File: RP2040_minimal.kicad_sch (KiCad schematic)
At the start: 34 parts

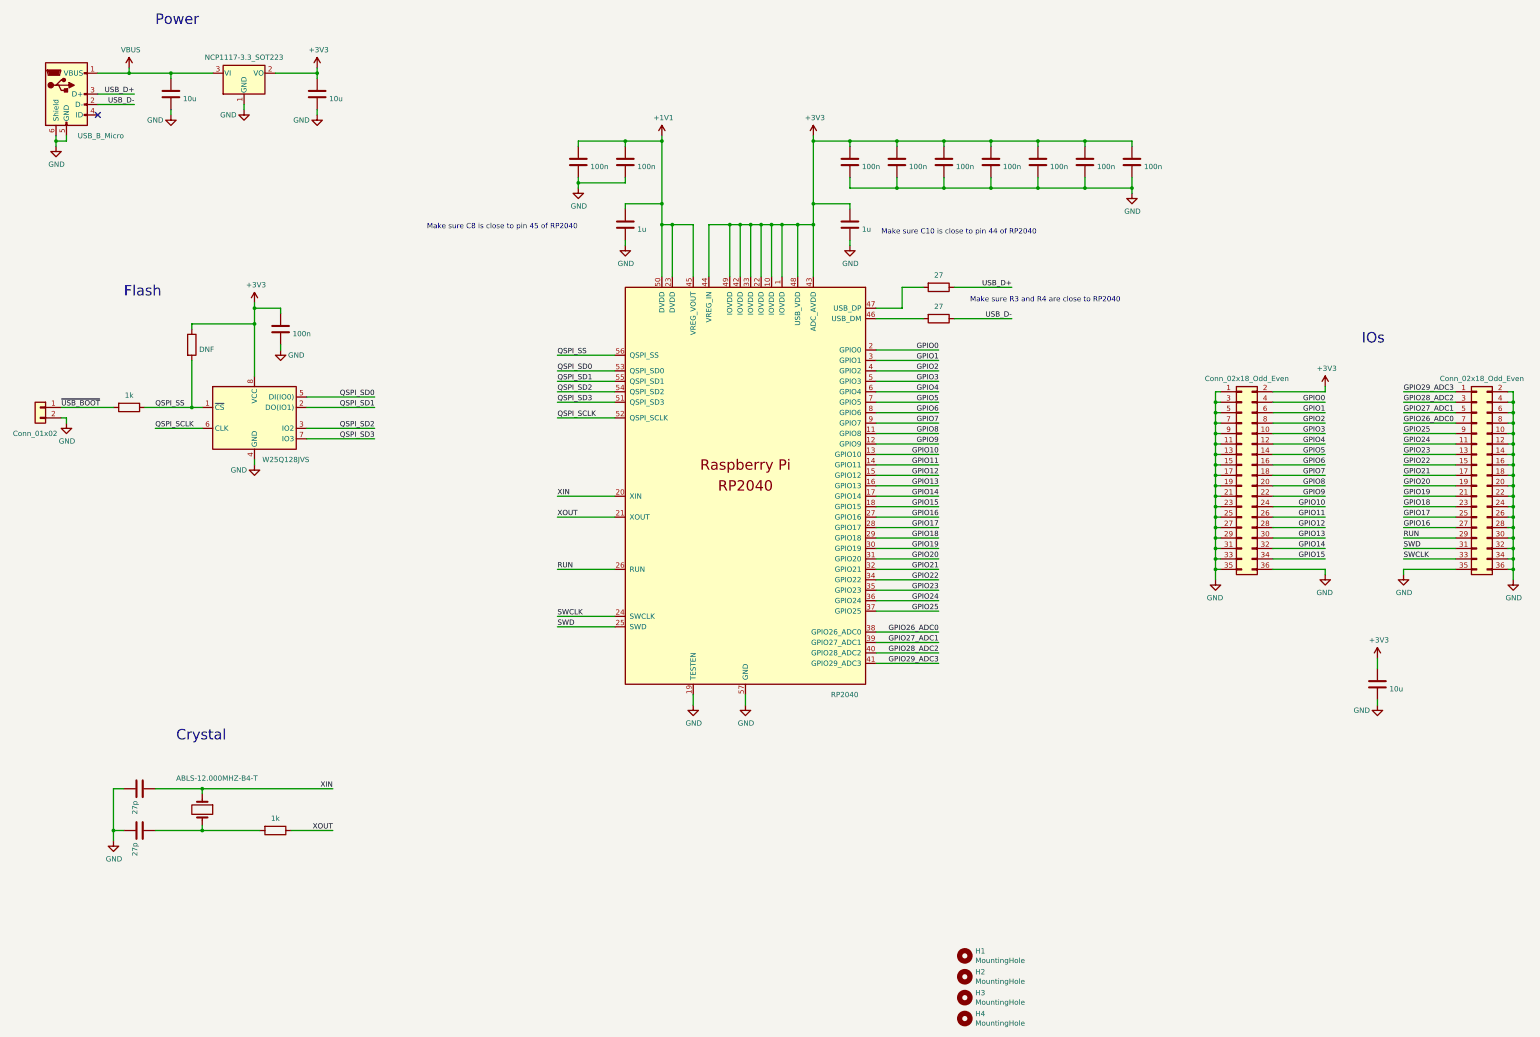
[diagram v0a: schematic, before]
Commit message: Updated sheet information, renumbered annotation for capacitors.
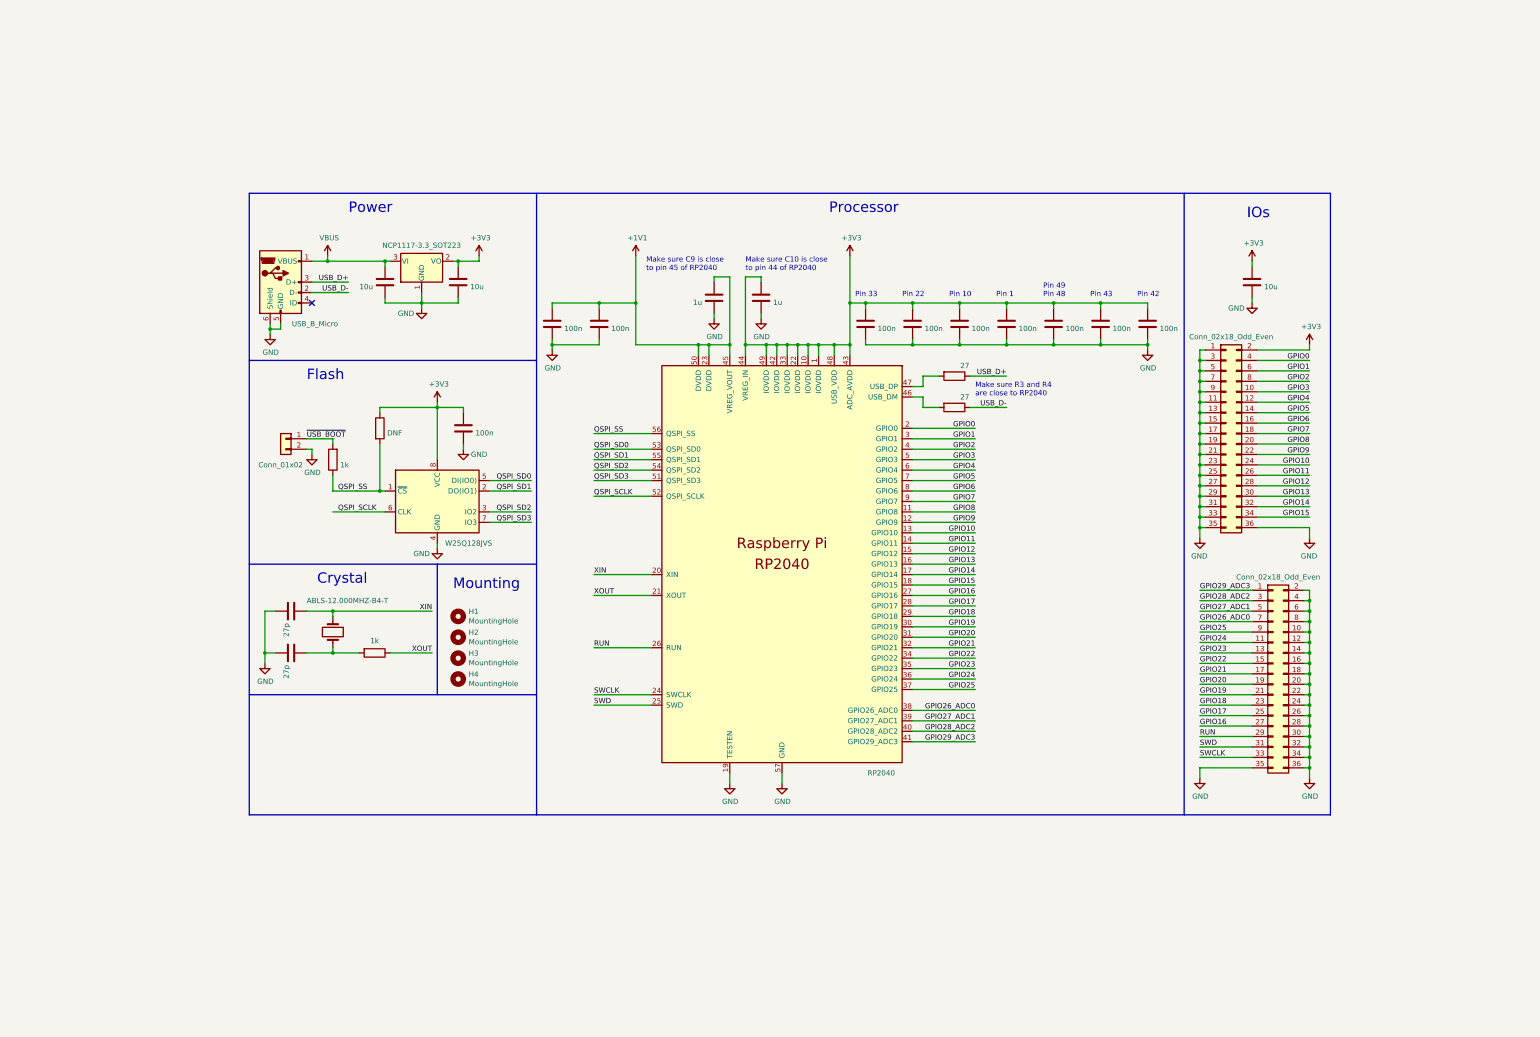
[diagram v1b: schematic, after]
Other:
- note added: "Make sure C9 is close to pin 45 of RP2040"
- note added: "Mounting"
- note added: "Pin 1"
- note added: "Pin 10"
- note added: "Pin 22"
- note added: "Pin 33"
- note added: "Pin 42"
- note added: "Pin 43"
- note added: "Pin 49 Pin 48"
- note added: "Processor"
- note removed: "Make sure C8 is close to pin 45 of RP2040"
- company: Raspberry Pi (Trading) Ltd -> AET Tech
- moved on the sheet: H1, H2, H3, H4

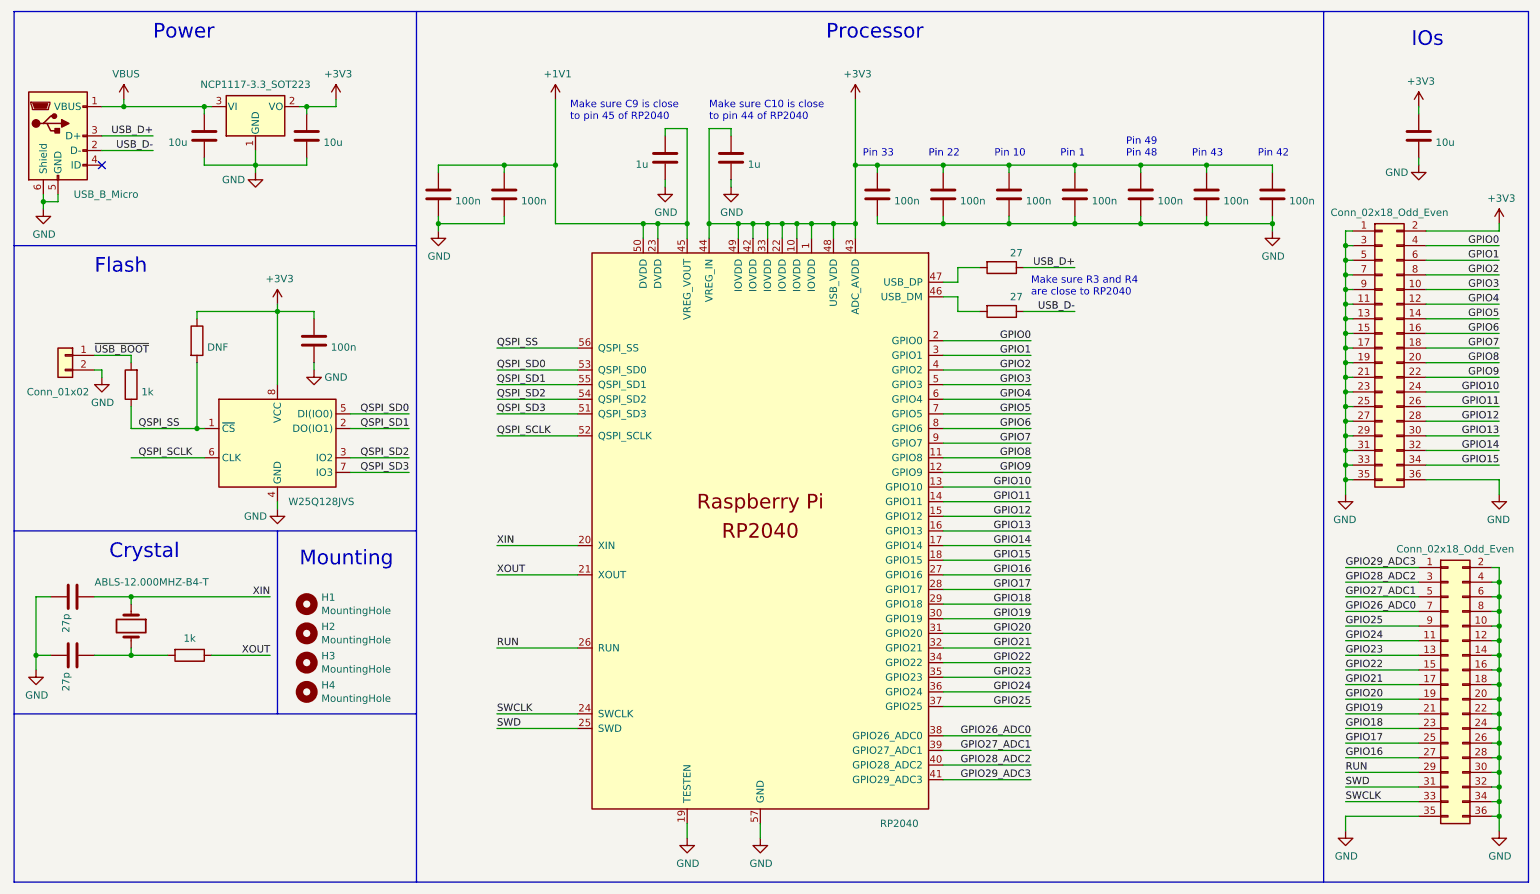
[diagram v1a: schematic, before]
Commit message: Replaced USB Micro A receptacle with USB C Added 5k1 resistors for UFP identification Added jumpers connecting CC1 to GPIO21, CC2 to GPIO22, SBU2 to GPIO0,   and SBU2 to GPIO1. Added jumper for VBUS
Updated README.md
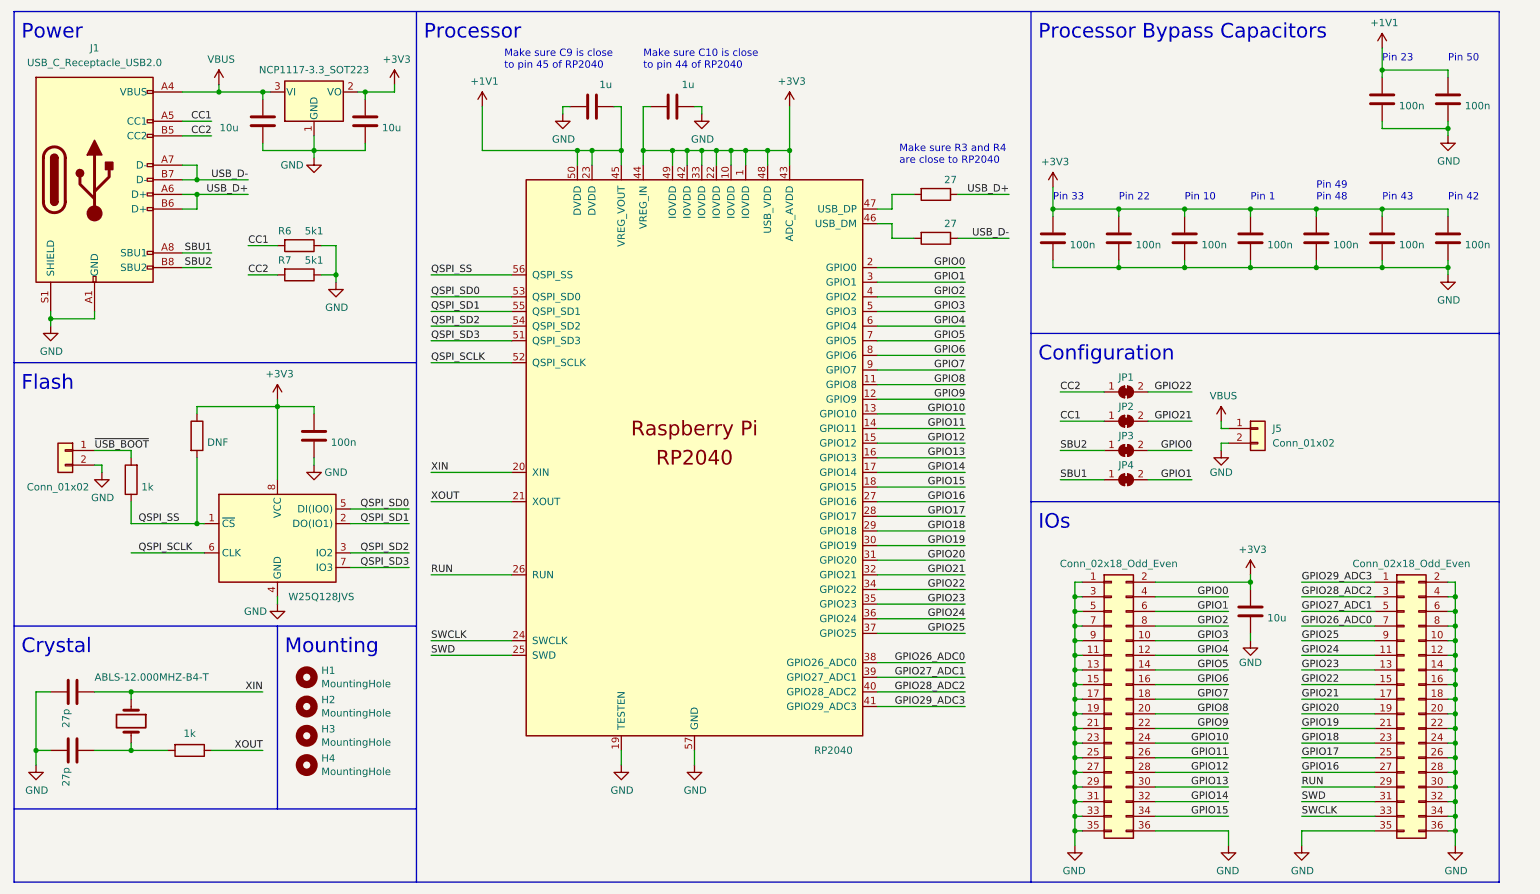
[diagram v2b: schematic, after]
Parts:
- removed ?: USB_B_Micro, RP2040_minimal:USB_Micro-B_Amphenol_10103594-0001LF_Horizontal_modified, symbol RP2040_minimal-rescue:USB_B_Micro-Connector
- added J1: USB_C_Receptacle_USB2.0, Connector_USB:USB_C_Receptacle_JAE_DX07S016JA1R1500, symbol Connector:USB_C_Receptacle_USB2.0
- added J5: Conn_01x02, Connector_PinHeader_2.54mm:PinHeader_1x02_P2.54mm_Vertical, symbol Connector_Generic:Conn_01x02
- added JP1, JP2, JP3, JP4: SolderJumper_2_Bridged, Jumper:SolderJumper-2_P1.3mm_Bridged_RoundedPad1.0x1.5mm, symbol Jumper:SolderJumper_2_Bridged
- added R6, R7: 5k1, Capacitor_SMD:C_0402_1005Metric, symbol Device:R
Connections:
- net GND: now also J1.A1 (GND), J1.A12 (GND), J1.B1 (GND), J1.B12 (GND), J1.S1 (SHIELD), J5.2 (Pin_2), R6.1, R7.1
- net GPIO0: now also JP3.2 (B)
- net GPIO1: now also JP4.2 (B)
- net GPIO21: now also JP2.2 (B)
- net GPIO22: now also JP1.2 (B)
- net USB_D+: now also J1.A6 (D+), J1.B6 (D+)
- net USB_D-: now also J1.A7 (D-), J1.B7 (D-)
- net VBUS: now also J1.A4 (VBUS), J1.A9 (VBUS), J1.B4 (VBUS), J1.B9 (VBUS), J5.1 (Pin_1)
- new net CC1: J1.A5 (CC1), JP2.1 (A), R6.2
- new net CC2: J1.B5 (CC2), JP1.1 (A), R7.2
- new net SBU1: J1.A8 (SBU1), JP4.1 (A)
- new net SBU2: J1.B8 (SBU2), JP3.1 (A)
- no-connect marks 1 -> 0
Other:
- note added: "Configuration"
- note added: "Pin 23"
- note added: "Pin 50"
- note added: "Processor Bypass Capacitors"
- moved on the sheet: H1, H2, H3, H4
